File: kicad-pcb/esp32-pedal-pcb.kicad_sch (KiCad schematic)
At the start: 54 parts, among them J1 USB4110-GF-A, SW1 B2B-PH-K-S(LF)(SN), SW2 B2B-PH-K-S(LF)(SN), U1 MCP73871T-2CCI/ML, U2 TLV75733PDBV, U3 ESP32-S3-WROOM-1-N8, U4 TPD2EUSB30ADRTR, U6 TPS2553DBVR

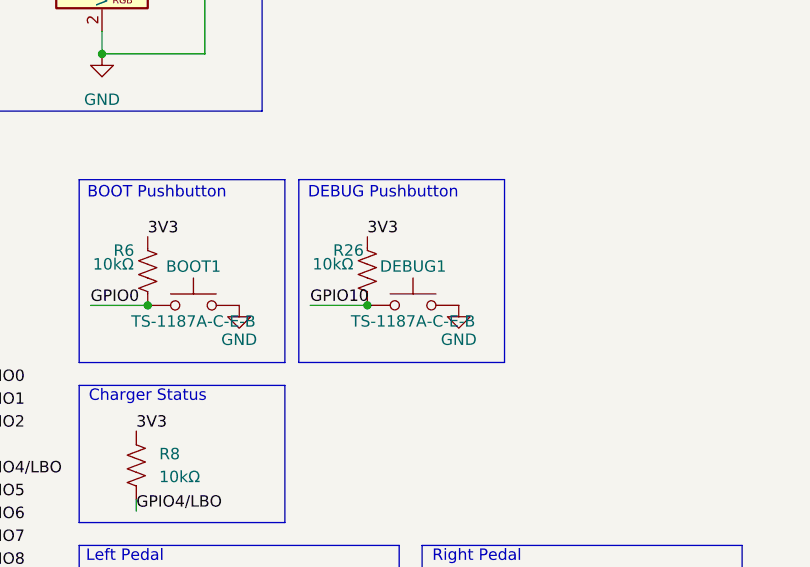
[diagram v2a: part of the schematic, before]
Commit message: Unify debug messaging across all devices using shared DebugService
- Enhanced DebugService to support both EspNowTransport (transmitters) and ReceiverEspNowTransport (receiver) via function pointers
- Migrated receiver from DebugMonitor module to shared DebugService
- Added setDeviceType() to correctly tag debug messages with device type
- Fixed grace period timing issue when clearing MAC addresses (use currentTime instead of millis())
- Improved debug messages to distinguish between no transmitters loaded vs no replies
- All devices now use the same code for sending debug messages to debug monitor
- Message buffering works consistently across all device types
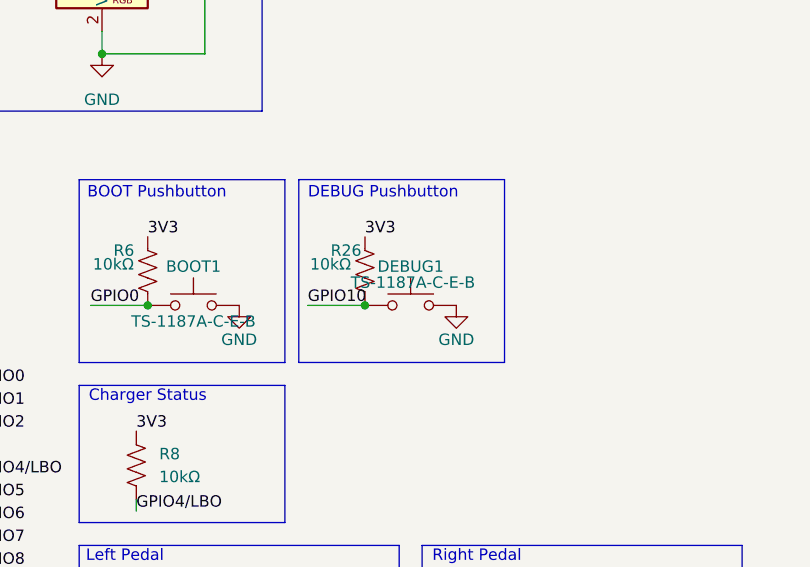
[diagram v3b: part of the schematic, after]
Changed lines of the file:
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@@
 	)
 	(junction
-		(at 199.6628 173.9821)
+		(at 139.7 135.89)
 		(diameter 0)
 		(color 0 0 0 0)
 	)
 	(junction
-		(at 139.7 135.89)
+		(at 220.98 218.44)
 		(diameter 0)
 		(color 0 0 0 0)
 	)
 	(junction
-		(at 220.98 218.44)
+		(at 199.39 173.99)
 		(diameter 0)
 		(color 0 0 0 0)
@@
 	(wire
 		(pts
+			(xy 193.04 173.99) (xy 199.39 173.99)
+		)
+		(stroke
+			(width 0)
+			(type default)
+		)
+	)
+	(wire
+		(pts
 			(xy 105.41 46.99) (xy 105.41 50.8)
 		)
@@
 	(wire
 		(pts
-			(xy 193.3128 173.9821) (xy 199.6628 173.9821)
-		)
-		(stroke
-			(width 0)
-			(type default)
-		)
-	)
-	(wire
-		(pts
 			(xy 41.91 100.33) (xy 41.91 102.87)
 		)
@@
 		)
 	)
+	(label "3V3"
+		(at 199.39 166.37 0)
+		(effects
+			(font
+				(size 1.27 1.27)
+			)
+			(justify left bottom)
+		)
+	)
 	(label "TPS OUT"
 		(at 95.25 49.53 0)
@@
 		)
 	)
-	(label "3V3"
-		(at 199.6628 166.3621 0)
-		(effects
-			(font
-				(size 1.27 1.27)
-			)
-			(justify left bottom)
-		)
-	)
 	(label "GPIO10"
-		(at 193.3128 173.9821 0)
+		(at 193.04 173.99 0)
 		(effects
 			(font
@@
 	(symbol
 		(lib_id "Device:R_US")
-		(at 199.6628 170.1721 0)
+		(at 199.39 170.18 0)
 		(unit 1)
 		(exclude_from_sim no)
@@
 		(dnp no)
 		(property "Reference" "R26"
-			(at 195.8528 167.8861 0)
+			(at 195.58 167.894 0)
 			(effects
 				(font
@@
 		)
 		(property "Value" "10kΩ"
-			(at 193.5668 169.4101 0)
+			(at 193.294 169.418 0)
 			(effects
 				(font
@@
 		)
 		(property "Footprint" "Resistor_SMD:R_0603_1608Metric"
-			(at 200.6788 170.4261 90)
+			(at 200.406 170.434 90)
 			(effects
 				(font
@@
 		)
 		(property "Datasheet" "~"
-			(at 199.6628 170.1721 0)
+			(at 199.39 170.18 0)
 			(effects
 				(font
@@
 		)
 		(property "Description" "Resistor, US symbol"
-			(at 199.6628 170.1721 0)
+			(at 199.39 170.18 0)
 			(effects
 				(font
@@
 		)
 		(property "Sim.Device" ""
-			(at 199.6628 170.1721 0)
+			(at 199.39 170.18 0)
 			(effects
 				(font
@@
 		)
 		(property "Sim.Type" ""
-			(at 199.6628 170.1721 0)
+			(at 199.39 170.18 0)
 			(effects
 				(font
@@
 	(symbol
 		(lib_id "Switch:SW_Push")
-		(at 204.7428 173.9821 0)
+		(at 204.47 173.99 0)
 		(unit 1)
 		(exclude_from_sim no)
@@
 		(dnp no)
 		(property "Reference" "DEBUG1"
-			(at 204.7428 169.6641 0)
+			(at 204.47 169.672 0)
 			(effects
 				(font
@@
 		)
 		(property "Value" "TS-1187A-C-E-B"
-			(at 204.7428 175.7601 0)
+			(at 204.724 171.45 0)
 			(effects
 				(font
@@
 		)
 		(property "Footprint" "Button_Switch_SMD:SW_Push_1P1T_XKB_TS-1187A"
-			(at 204.7428 168.9021 0)
+			(at 204.47 168.91 0)
 			(effects
 				(font
@@
 		)
 		(property "Datasheet" "~"
-			(at 204.7428 168.9021 0)
+			(at 204.47 168.91 0)
 			(effects
 				(font
@@
 		)
 		(property "Description" "Push button switch, generic, two pins"
-			(at 204.7428 173.9821 0)
+			(at 204.47 173.99 0)
 			(effects
 				(font
@@
 		)
 		(property "Sim.Device" ""
-			(at 204.7428 173.9821 0)
+			(at 204.47 173.99 0)
 			(effects
 				(font
@@
 		)
 		(property "Sim.Type" ""
-			(at 204.7428 173.9821 0)
+			(at 204.47 173.99 0)
 			(effects
 				(font
@@
 	(symbol
 		(lib_id "power:GND")
-		(at 209.8228 173.9821 0)
+		(at 209.55 173.99 0)
 		(unit 1)
 		(exclude_from_sim no)
@@
 		(dnp no)
 		(property "Reference" "#PWR021"
-			(at 209.8228 180.3321 0)
+			(at 209.55 180.34 0)
 			(effects
 				(font
@@
 		)
 		(property "Value" "GND"
-			(at 209.8228 177.7921 0)
+			(at 209.55 177.8 0)
 			(effects
 				(font
@@
 		)
 		(property "Footprint" ""
-			(at 209.8228 173.9821 0)
+			(at 209.55 173.99 0)
 			(effects
 				(font
@@
 		)
 		(property "Datasheet" ""
-			(at 209.8228 173.9821 0)
+			(at 209.55 173.99 0)
 			(effects
 				(font
@@
 		)
 		(property "Description" "Power symbol creates a global label with name \"GND\" , ground"
-			(at 209.8228 173.9821 0)
+			(at 209.55 173.99 0)
 			(effects
 				(font
